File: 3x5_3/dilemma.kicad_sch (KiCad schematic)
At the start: 91 parts, among them J5001 BATTERY_CONN_DEANS, J5011 BATTERY_CONN_DEANS, SW101 NA_SW_Push, SW102 NA_SW_Push, SW103 NA_SW_Push, SW104 NA_SW_Push, SW105 NA_SW_Push, SW106 NA_SW_Push, SW107 NA_SW_Push, SW108 NA_SW_Push, SW109 NA_SW_Push, SW112 NA_SW_Push, SW113 NA_SW_Push, SW114 NA_SW_Push, SW115 NA_SW_Push, SW116 NA_SW_Push, SW117 NA_SW_Push, SW118 NA_SW_Push, SW119 NA_SW_Push, SW3001 NA_SW_Push, SW5002 NA_SW_Push, SW5003 NA_SW_Push, SW5004 NA_SW_Push, SW5005 NA_SW_Push, SW5006 NA_SW_Push, SW5007 NA_SW_Push, SW5008 NA_SW_Push, SW5009 NA_SW_Push, SW5010 NA_SW_Push, SW5011 NA_SW_Push, SW5012 NA_SW_Push, SW5013 NA_SW_Push, SW5014 NA_SW_Push, SW5015 NA_SW_Push, SW5016 NA_SW_Push, SW5017 NA_SW_Push, SW5018 NA_SW_Push, SW5019 NA_SW_Push, SW5021 SW_SPST, SW5022 SW_SPST, U5001 eliteC, U5007 eliteC

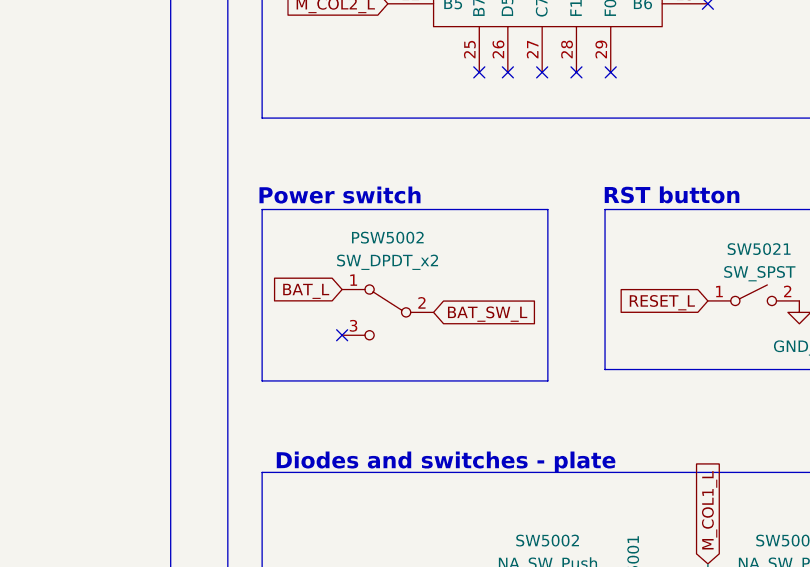
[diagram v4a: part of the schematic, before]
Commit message: fix jst clearance
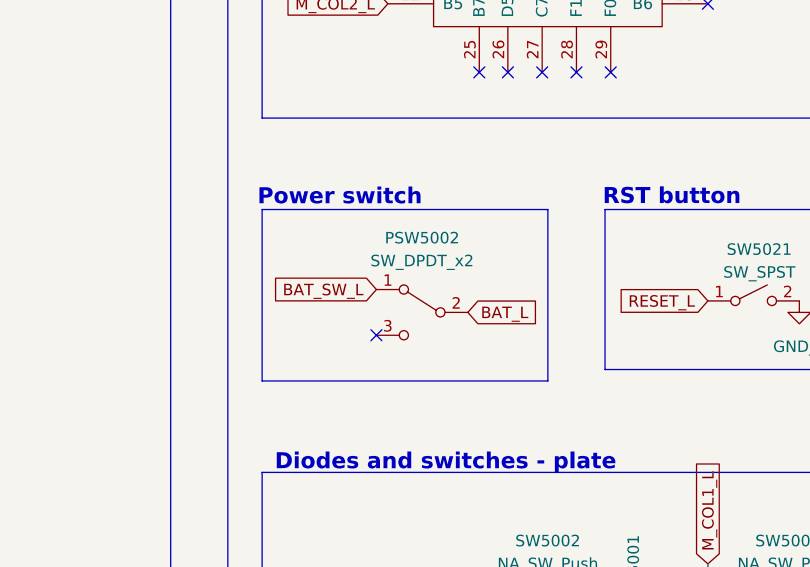
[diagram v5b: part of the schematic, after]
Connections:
- net BAT_L: now also PSW5002.2 (B); no longer PSW5002.1 (A)
- net BAT_SW_L: now also PSW5002.1 (A); no longer PSW5002.2 (B)
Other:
- moved on the sheet: PSW5002
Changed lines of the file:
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@@
 	)
 	(no_connect
-		(at 224.79 124.46)
+		(at 228.6 124.46)
 	)
 	(no_connect
@@
 	(global_label "BAT_L"
 		(shape input)
-		(at 224.79 119.38 180)
+		(at 238.76 121.92 0)
 		(effects
 			(font
 				(size 1.27 1.27)
 			)
-			(justify right)
+			(justify left)
 		)
 		(property "Intersheetrefs" "${INTERSHEET_REFS}"
-			(at 347.98 250.19 0)
+			(at 115.57 -8.89 0)
 			(effects
 				(font
@@
 	(global_label "BAT_SW_L"
 		(shape input)
-		(at 234.95 121.92 0)
+		(at 228.6 119.38 180)
 		(effects
 			(font
 				(size 1.27 1.27)
 			)
-			(justify left)
+			(justify right)
 		)
 		(property "Intersheetrefs" "${INTERSHEET_REFS}"
-			(at 111.76 -8.89 0)
+			(at 351.79 250.19 0)
 			(effects
 				(font
@@
 	(symbol
 		(lib_id "jiran-ble:SW_DPDT")
-		(at 228.6 121.92 0)
+		(at 232.41 121.92 0)
 		(mirror y)
 		(unit 1)
@@
 		(dnp no)
 		(property "Reference" "PSW5002"
-			(at 229.87 113.665 0)
+			(at 233.68 113.665 0)
 			(effects
 				(font
@@
 		)
 		(property "Value" "SW_DPDT_x2"
-			(at 229.87 116.205 0)
+			(at 233.68 116.205 0)
 			(effects
 				(font
@@
 		)
 		(property "Footprint" "local-libraries:Switch_MSK-12C01-07"
-			(at 227.965 114.3 0)
+			(at 231.775 114.3 0)
 			(effects
 				(font
@@
 		)
 		(property "Datasheet" ""
-			(at 227.965 114.3 0)
+			(at 231.775 114.3 0)
 			(effects
 				(font
@@
 		)
 		(property "Description" ""
-			(at 228.6 121.92 0)
+			(at 232.41 121.92 0)
 			(effects
 				(font
@@
 		)
 		(property "LCSC" "C431540"
-			(at 228.6 121.92 0)
+			(at 232.41 121.92 0)
 			(effects
 				(font

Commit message: choc v2
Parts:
- SW101, SW102, SW103, SW104, SW105, SW106, SW107, SW108, SW109, SW112, SW113, SW114, SW115, SW116, SW117, SW118, SW119, SW3001, SW5002, SW5003, SW5004, SW5005, SW5006, SW5007, SW5008, SW5009, SW5010, SW5011, SW5012, SW5013, SW5014, SW5015, SW5016, SW5017, SW5018, SW5019: footprint local-libraries:SW_MX_choc -> local-libraries:SW_Kailh_Choc_V2_1.00u
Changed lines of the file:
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@@
 			)
 		)
-		(property "Footprint" "local-libraries:SW_MX_choc"
+		(property "Footprint" "local-libraries:SW_Kailh_Choc_V2_1.00u"
 			(at 300.99 180.34 0)
 			(effects
@@
 			)
 		)
-		(property "Footprint" "local-libraries:SW_MX_choc"
+		(property "Footprint" "local-libraries:SW_Kailh_Choc_V2_1.00u"
 			(at 247.65 160.02 0)
 			(effects
@@
 			)
 		)
-		(property "Footprint" "local-libraries:SW_MX_choc"
+		(property "Footprint" "local-libraries:SW_Kailh_Choc_V2_1.00u"
 			(at 50.8 179.07 0)
 			(effects
@@
 			)
 		)
-		(property "Footprint" "local-libraries:SW_MX_choc"
+		(property "Footprint" "local-libraries:SW_Kailh_Choc_V2_1.00u"
 			(at 104.14 168.91 0)
 			(effects
@@
 			)
 		)
-		(property "Footprint" "local-libraries:SW_MX_choc"
+		(property "Footprint" "local-libraries:SW_Kailh_Choc_V2_1.00u"
 			(at 77.47 158.75 0)
 			(effects
@@
 			)
 		)
-		(property "Footprint" "local-libraries:SW_MX_choc"
+		(property "Footprint" "local-libraries:SW_Kailh_Choc_V2_1.00u"
 			(at 300.99 170.18 0)
 			(effects
@@
 			)
 		)
-		(property "Footprint" "local-libraries:SW_MX_choc"
+		(property "Footprint" "local-libraries:SW_Kailh_Choc_V2_1.00u"
 			(at 157.48 168.91 0)
 			(effects
@@
 			)
 		)
-		(property "Footprint" "local-libraries:SW_MX_choc"
+		(property "Footprint" "local-libraries:SW_Kailh_Choc_V2_1.00u"
 			(at 50.8 158.75 0)
 			(effects
@@
 			)
 		)
-		(property "Footprint" "local-libraries:SW_MX_choc"
+		(property "Footprint" "local-libraries:SW_Kailh_Choc_V2_1.00u"
 			(at 300.99 149.86 0)
 			(effects
@@
 			)
 		)
-		(property "Footprint" "local-libraries:SW_MX_choc"
+		(property "Footprint" "local-libraries:SW_Kailh_Choc_V2_1.00u"
 			(at 157.48 148.59 0)
 			(effects
@@
 			)
 		)
-		(property "Footprint" "local-libraries:SW_MX_choc"
+		(property "Footprint" "local-libraries:SW_Kailh_Choc_V2_1.00u"
 			(at 157.48 158.75 0)
 			(effects
@@
 			)
 		)
-		(property "Footprint" "local-libraries:SW_MX_choc"
+		(property "Footprint" "local-libraries:SW_Kailh_Choc_V2_1.00u"
 			(at 77.47 148.59 0)
 			(effects
@@
 			)
 		)
-		(property "Footprint" "local-libraries:SW_MX_choc"
+		(property "Footprint" "local-libraries:SW_Kailh_Choc_V2_1.00u"
 			(at 274.32 180.34 0)
 			(effects
@@
 			)
 		)
-		(property "Footprint" "local-libraries:SW_MX_choc"
+		(property "Footprint" "local-libraries:SW_Kailh_Choc_V2_1.00u"
 			(at 130.81 168.91 0)
 			(effects
@@
 			)
 		)
-		(property "Footprint" "local-libraries:SW_MX_choc"
+		(property "Footprint" "local-libraries:SW_Kailh_Choc_V2_1.00u"
 			(at 77.47 168.91 0)
 			(effects
@@
 			)
 		)
-		(property "Footprint" "local-libraries:SW_MX_choc"
+		(property "Footprint" "local-libraries:SW_Kailh_Choc_V2_1.00u"
 			(at 247.65 149.86 0)
 			(effects
@@
 			)
 		)
-		(property "Footprint" "local-libraries:SW_MX_choc"
+		(property "Footprint" "local-libraries:SW_Kailh_Choc_V2_1.00u"
 			(at 327.66 149.86 0)
 			(effects
@@
 			)
 		)
-		(property "Footprint" "local-libraries:SW_MX_choc"
+		(property "Footprint" "local-libraries:SW_Kailh_Choc_V2_1.00u"
 			(at 354.33 160.02 0)
 			(effects
@@
 			)
 		)
-		(property "Footprint" "local-libraries:SW_MX_choc"
+		(property "Footprint" "local-libraries:SW_Kailh_Choc_V2_1.00u"
 			(at 247.65 170.18 0)
 			(effects
@@
 			)
 		)
-		(property "Footprint" "local-libraries:SW_MX_choc"
+		(property "Footprint" "local-libraries:SW_Kailh_Choc_V2_1.00u"
 			(at 130.81 158.75 0)
 			(effects
@@
 			)
 		)
-		(property "Footprint" "local-libraries:SW_MX_choc"
+		(property "Footprint" "local-libraries:SW_Kailh_Choc_V2_1.00u"
 			(at 104.14 148.59 0)
 			(effects
@@
 			)
 		)
-		(property "Footprint" "local-libraries:SW_MX_choc"
+		(property "Footprint" "local-libraries:SW_Kailh_Choc_V2_1.00u"
 			(at 354.33 170.18 0)
 			(effects
@@
 			)
 		)
-		(property "Footprint" "local-libraries:SW_MX_choc"
+		(property "Footprint" "local-libraries:SW_Kailh_Choc_V2_1.00u"
 			(at 130.81 148.59 0)
 			(effects
@@
 			)
 		)
-		(property "Footprint" "local-libraries:SW_MX_choc"
+		(property "Footprint" "local-libraries:SW_Kailh_Choc_V2_1.00u"
 			(at 274.32 160.02 0)
 			(effects
@@
 			)
 		)
-		(property "Footprint" "local-libraries:SW_MX_choc"
+		(property "Footprint" "local-libraries:SW_Kailh_Choc_V2_1.00u"
 			(at 104.14 179.07 0)
 			(effects
@@
 			)
 		)
-		(property "Footprint" "local-libraries:SW_MX_choc"
+		(property "Footprint" "local-libraries:SW_Kailh_Choc_V2_1.00u"
 			(at 274.32 149.86 0)
 			(effects
@@
 			)
 		)
-		(property "Footprint" "local-libraries:SW_MX_choc"
+		(property "Footprint" "local-libraries:SW_Kailh_Choc_V2_1.00u"
 			(at 354.33 149.86 0)
 			(effects
@@
 			)
 		)
-		(property "Footprint" "local-libraries:SW_MX_choc"
+		(property "Footprint" "local-libraries:SW_Kailh_Choc_V2_1.00u"
 			(at 300.99 160.02 0)
 			(effects
@@
 			)
 		)
-		(property "Footprint" "local-libraries:SW_MX_choc"
+		(property "Footprint" "local-libraries:SW_Kailh_Choc_V2_1.00u"
 			(at 327.66 170.18 0)
 			(effects
@@
 			)
 		)
-		(property "Footprint" "local-libraries:SW_MX_choc"
+		(property "Footprint" "local-libraries:SW_Kailh_Choc_V2_1.00u"
 			(at 247.65 180.34 0)
 			(effects
@@
 			)
 		)
-		(property "Footprint" "local-libraries:SW_MX_choc"
+		(property "Footprint" "local-libraries:SW_Kailh_Choc_V2_1.00u"
 			(at 104.14 158.75 0)
 			(effects
@@
 			)
 		)
-		(property "Footprint" "local-libraries:SW_MX_choc"
+		(property "Footprint" "local-libraries:SW_Kailh_Choc_V2_1.00u"
 			(at 327.66 160.02 0)
 			(effects
@@
 			)
 		)
-		(property "Footprint" "local-libraries:SW_MX_choc"
+		(property "Footprint" "local-libraries:SW_Kailh_Choc_V2_1.00u"
 			(at 50.8 168.91 0)
 			(effects
@@
 			)
 		)
-		(property "Footprint" "local-libraries:SW_MX_choc"
+		(property "Footprint" "local-libraries:SW_Kailh_Choc_V2_1.00u"
 			(at 50.8 148.59 0)
 			(effects
@@
 			)
 		)
-		(property "Footprint" "local-libraries:SW_MX_choc"
+		(property "Footprint" "local-libraries:SW_Kailh_Choc_V2_1.00u"
 			(at 274.32 170.18 0)
 			(effects
@@
 			)
 		)
-		(property "Footprint" "local-libraries:SW_MX_choc"
+		(property "Footprint" "local-libraries:SW_Kailh_Choc_V2_1.00u"
 			(at 77.47 179.07 0)
 			(effects

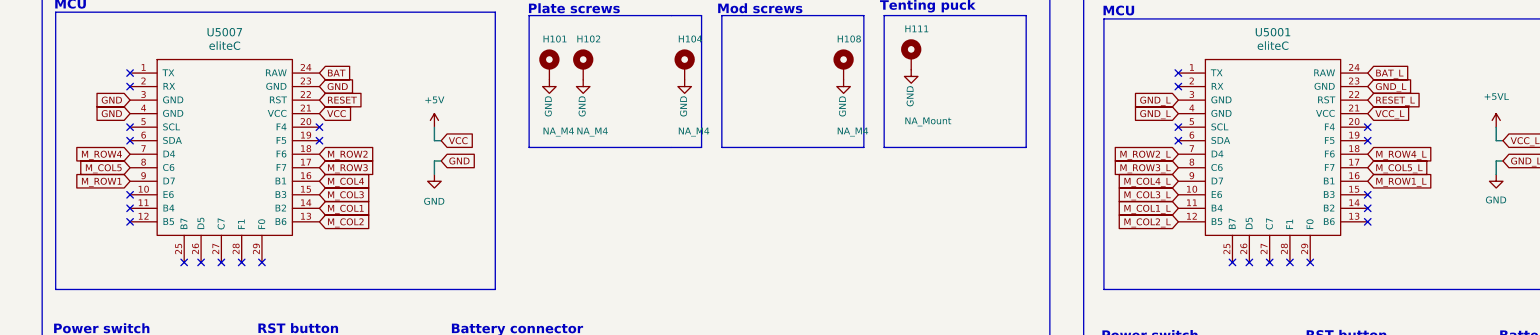
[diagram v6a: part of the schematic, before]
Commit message: antenna cutout
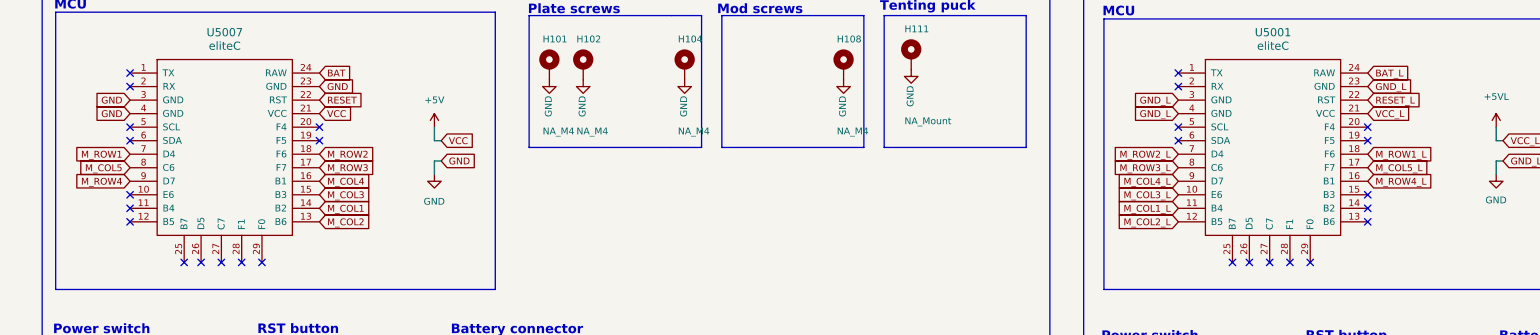
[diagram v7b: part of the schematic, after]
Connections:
- net M_ROW1: now also U5007.7 (D4); no longer U5007.9 (D7)
- net M_ROW1_L: now also U5001.18 (F6); no longer U5001.16 (B1)
- net M_ROW4: now also U5007.9 (D7); no longer U5007.7 (D4)
- net M_ROW4_L: now also U5001.16 (B1); no longer U5001.18 (F6)
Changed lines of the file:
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@@
 	(global_label "M_ROW4_L"
 		(shape input)
-		(at 265.43 74.93 0)
-		(effects
-			(font
-				(size 1.27 1.27)
-			)
-			(justify left)
-		)
-		(property "Intersheetrefs" "${INTERSHEET_REFS}"
-			(at 337.185 158.115 0)
+		(at 265.43 80.01 0)
+		(effects
+			(font
+				(size 1.27 1.27)
+			)
+			(justify left)
+		)
+		(property "Intersheetrefs" "${INTERSHEET_REFS}"
+			(at 337.185 163.195 0)
 			(effects
 				(font
@@
 	(global_label "M_ROW4"
 		(shape input)
-		(at 33.02 74.93 180)
-		(effects
-			(font
-				(size 1.27 1.27)
-			)
-			(justify right)
-		)
-		(property "Intersheetrefs" "${INTERSHEET_REFS}"
-			(at 3.81 20.32 0)
+		(at 33.02 80.01 180)
+		(effects
+			(font
+				(size 1.27 1.27)
+			)
+			(justify right)
+		)
+		(property "Intersheetrefs" "${INTERSHEET_REFS}"
+			(at 3.81 25.4 0)
 			(effects
 				(font
@@
 	(global_label "M_ROW1"
 		(shape input)
-		(at 33.02 80.01 180)
-		(effects
-			(font
-				(size 1.27 1.27)
-			)
-			(justify right)
-		)
-		(property "Intersheetrefs" "${INTERSHEET_REFS}"
-			(at 3.81 38.1 0)
+		(at 33.02 74.93 180)
+		(effects
+			(font
+				(size 1.27 1.27)
+			)
+			(justify right)
+		)
+		(property "Intersheetrefs" "${INTERSHEET_REFS}"
+			(at 3.81 33.02 0)
 			(effects
 				(font
@@
 	(global_label "M_ROW1_L"
 		(shape input)
-		(at 265.43 80.01 0)
-		(effects
-			(font
-				(size 1.27 1.27)
-			)
-			(justify left)
-		)
-		(property "Intersheetrefs" "${INTERSHEET_REFS}"
-			(at 342.9 116.84 0)
-			(effects
-				(font
+		(at 265.43 74.93 0)
+		(effects
+			(font
+				(size 1.27 1.27)
+			)
+			(justify left)
+		)
+		(property "Intersheetrefs" "${INTERSHEET_REFS}"
+			(at 342.9 111.76 0)
+			(effects
+				(font

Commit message: convert to reversible pcb
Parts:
- removed BT5001: Battery, 0xB2_drawings:LP602945-PCM-LD-A14348, symbol Device:Battery
- removed D5001, D5002, D5003, D5004, D5005, D5006, D5007, D5008, D5009, D5010, D5011, D5012, D5013, D5014, D5015, D5016, D5017, D5018: D, Diode_SMD:D_SOD-123, symbol Device:D
- removed H111, H5008: NA_Mount, local-libraries:Tenting_Puck, symbol Mechanical:MountingHole_Pad
- removed H5001, H5002, H5003, H5007: NA_M4, local-libraries:MountingHole_3mm_Pad_Via, symbol Mechanical:MountingHole_Pad
- removed J5001: BATTERY_CONN_DEANS, local-libraries:battery_connector_THT, symbol SparkFun-Connectors:BATTERY_CONN_DEANS
- removed PSW5002: SW_DPDT_x2, local-libraries:Switch_MSK-12C01-07, symbol jiran-ble:SW_DPDT
- removed SW5002, SW5003, SW5004, SW5005, SW5006, SW5007, SW5008, SW5009, SW5010, SW5011, SW5012, SW5013, SW5014, SW5015, SW5016, SW5017, SW5018, SW5019: NA_SW_Push, local-libraries:SW_Kailh_Choc_V2_1.00u, symbol Switch:SW_Push
- removed SW5021: SW_SPST, Library:PushSwitch, symbol Switch:SW_SPST
- removed U5001: eliteC, local-libraries:Sparkfun_Pro_Micro, symbol elite-C:eliteC
- D112, D115, D5031, D5032, D5033, D5034, D5035, D5036, D5037, D5038, D5039, D5040, D5041, D5042, D5043, D5044, D5045, D5046: footprint Diode_SMD:D_SOD-123 -> local-libraries:D_SOD-123_reversible
- J5011: footprint local-libraries:battery_connector_THT -> local-libraries:battery_pads_reversible
- PSW5001: footprint local-libraries:Switch_MSK-12C01-07 -> local-libraries:Switch_MSK-12C01-07_reversible
- SW101, SW102, SW103, SW104, SW105, SW106, SW107, SW108, SW109, SW112, SW113, SW114, SW115, SW116, SW117, SW118, SW119, SW3001: footprint local-libraries:SW_Kailh_Choc_V2_1.00u -> local-libraries:SW_Kailh_Choc_V2_1.00u_reversible
- SW5022: footprint Library:PushSwitch -> local-libraries:reset_switch_reversible
- U5007: footprint local-libraries:Sparkfun_Pro_Micro -> local-libraries:nice!nano_reversible
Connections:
- net M_COL1: now also U5007.16 (B1); no longer U5007.14 (B2)
- net M_COL2: now also U5007.15 (B3); no longer U5007.13 (B6)
- net M_COL3: now also U5007.18 (F6); no longer U5007.15 (B3)
- net M_COL4: now also U5007.19 (F5); no longer U5007.16 (B1)
- net M_ROW2: now also U5007.20 (F4); no longer U5007.18 (F6)
- net +5V: no longer names the net of U5007.21 (VCC)
- no-connect marks 31 -> 11
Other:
- note removed: "Left"
- note removed: "Mod screws"
- note removed: "Right"
- note removed: "Tenting puck"
- moved on the sheet: H102, H104, H108
